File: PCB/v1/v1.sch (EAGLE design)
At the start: 73 parts, among them U2 AT24C512C-SHD-B

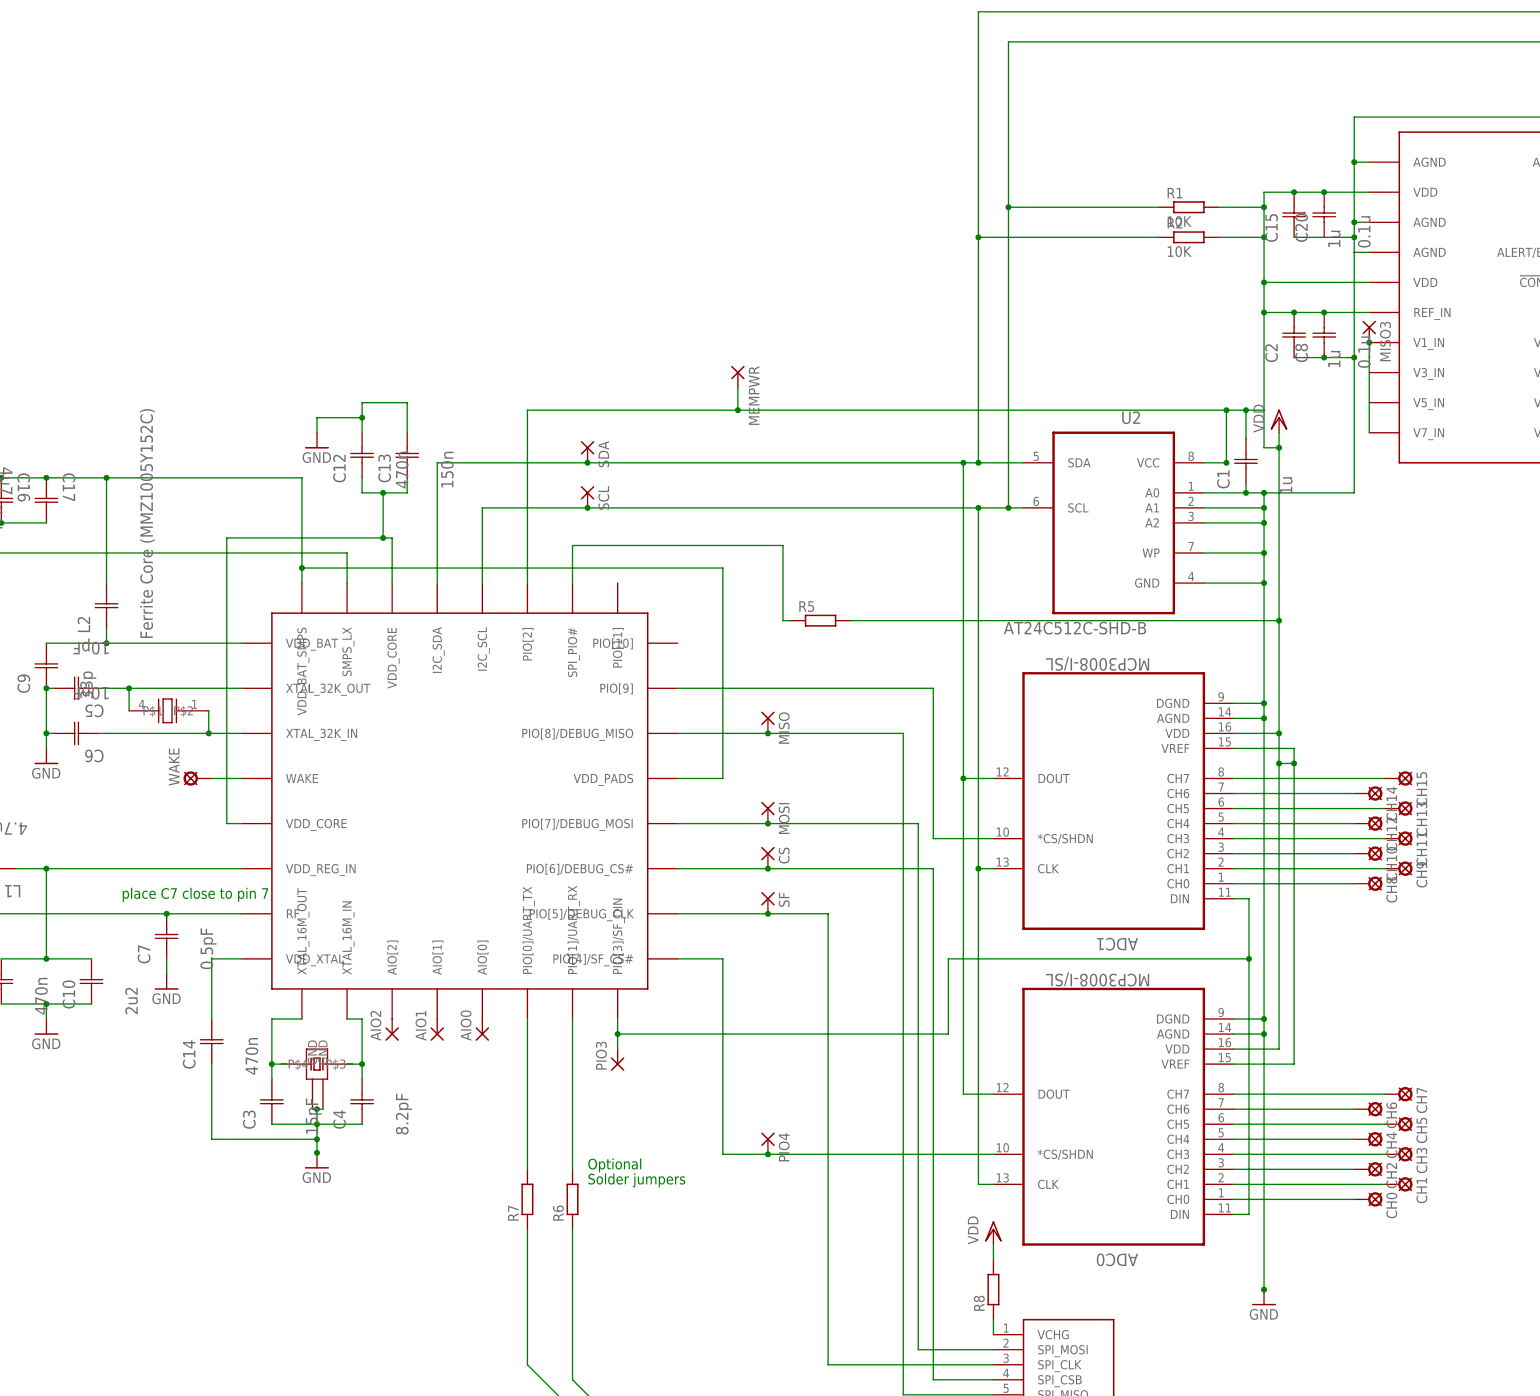
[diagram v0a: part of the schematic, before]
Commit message: ripped up. need to correct ADC package
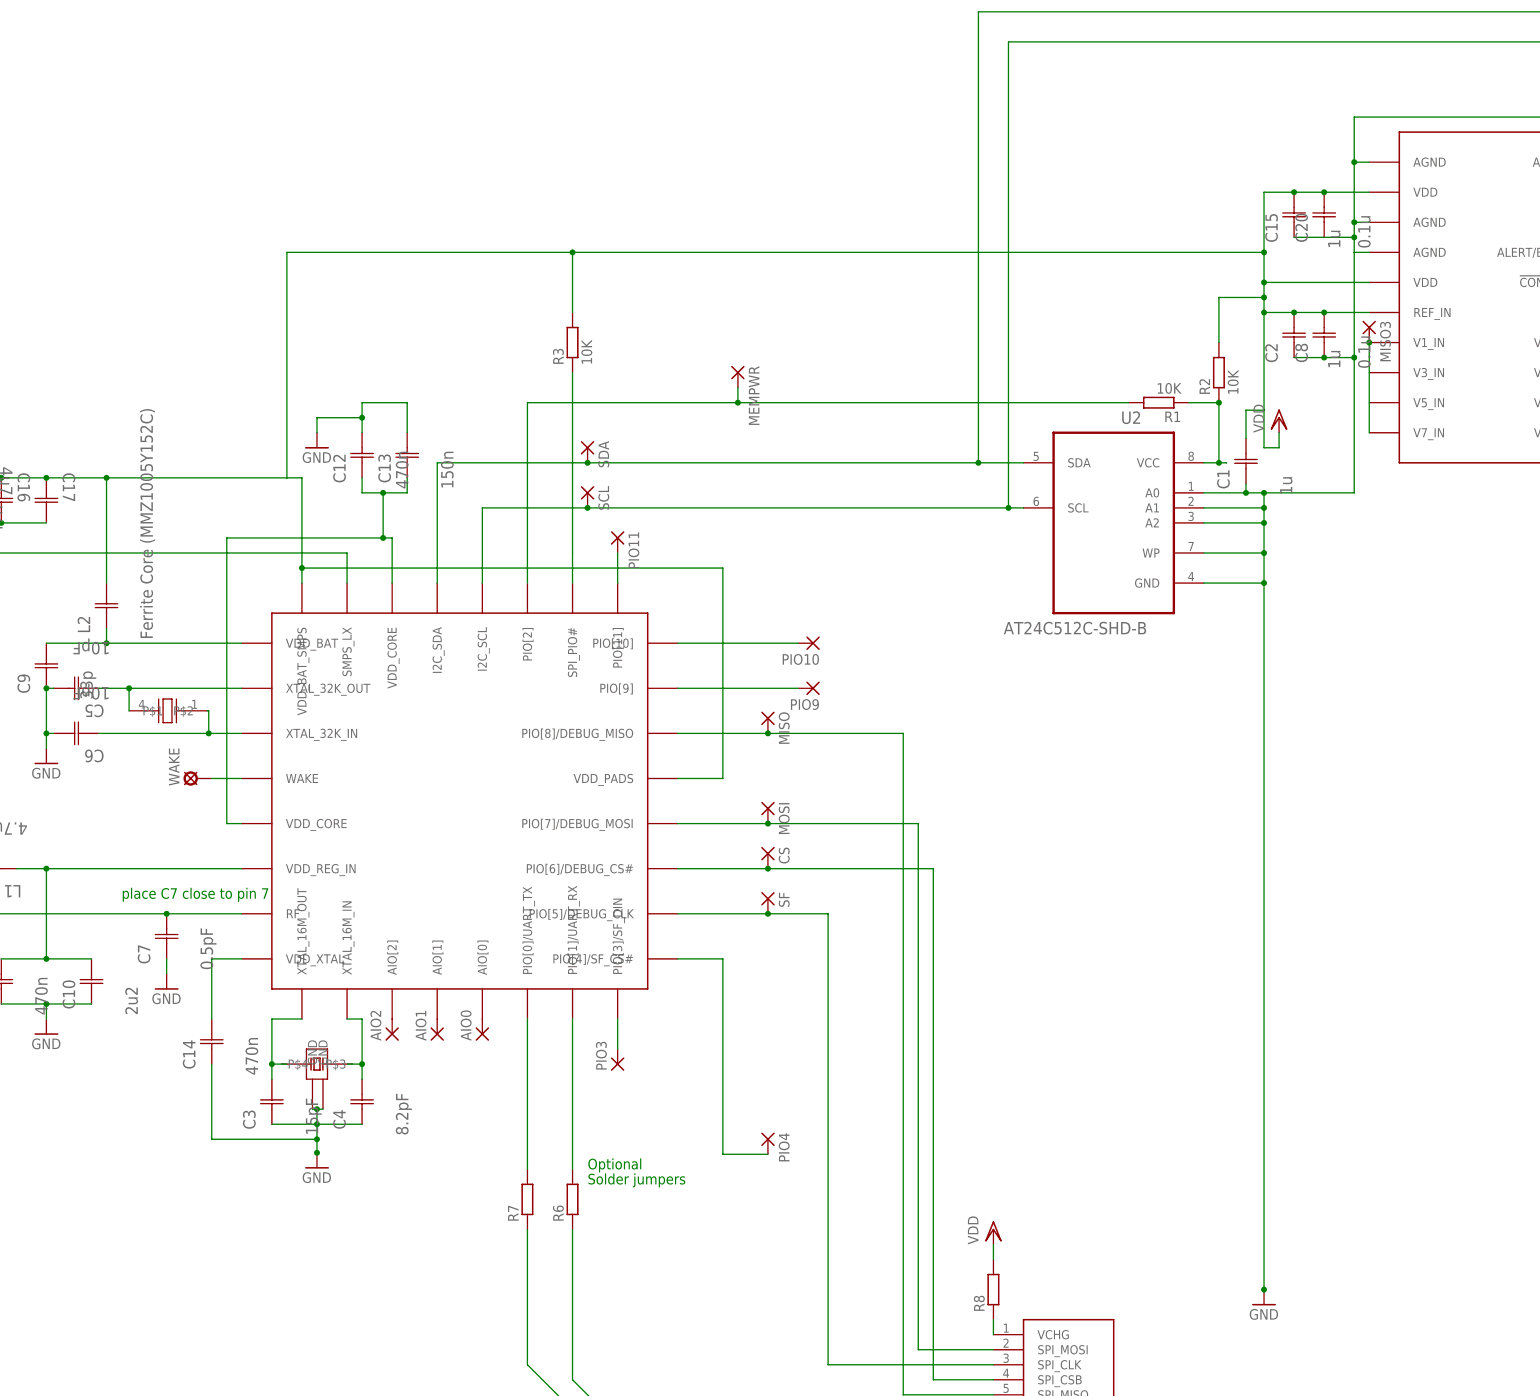
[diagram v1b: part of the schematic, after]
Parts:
- removed ADC0, ADC1: MCP3008-I/SL, Microchip_By_element14_Batch_1:MCP3008-I/SL
- removed CH0, CH1, CH10, CH11, CH12, CH13, CH14, CH15, CH2, CH3, CH4, CH5, CH6, CH7, CH8, CH9: LSP10, solpad:LSP10
- removed R5: (no value), eagle-ltspice:RR1206
- added PIO10, PIO11, PIO9: (no value), wirepad:1,6/0,8
- added R3: 10K, rcl:R-EU_R0402
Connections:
- removed net N$10: ADC1.CH6, CH14.MP
- removed net N$11: ADC1.CH5, CH13.MP
- removed net N$12: ADC1.CH4, CH12.MP
- removed net N$13: ADC1.CH3, CH11.MP
- removed net N$14: ADC1.CH2, CH10.MP
- removed net N$15: ADC1.CH1, CH9.MP
- removed net N$16: ADC1.CH0, CH8.MP
- removed net N$24: ADC1.*CS/SHDN, U$1.PIO[9]
- removed net N$34: C16.C1, C17.C1, C18.C2, C19.C2, L2.C2, U$1.VDD_BAT_SMPS, U$1.VDD_PADS, U$6.POS, VPLUS.MP
- removed net N$6: ADC0.CH2, CH2.MP
- removed net N$7: ADC0.CH1, CH1.MP
- removed net N$8: ADC0.CH0, CH0.MP
- removed net N$9: ADC1.CH7, CH15.MP
- net GND: no longer ADC0.AGND, ADC0.DGND, ADC1.AGND, ADC1.DGND
- net N$1: now also PIO11.P, U$1.PIO[11]; no longer ADC0.CH7, CH7.MP
- net N$2: now also PIO9.P, U$1.PIO[9]; no longer ADC0.CH6, CH6.MP
- net N$23: no longer ADC0.DIN, ADC1.DIN
- net N$25: no longer ADC0.*CS/SHDN
- net N$3: now also MEMPWR.P, R1.2, U$1.PIO[2]; no longer ADC0.CH5, CH5.MP
- net N$4: now also R1.1, R2.1, U2.VCC; no longer ADC0.CH4, CH4.MP
- net N$45: now also R3.1; no longer R5.1
- net N$5: now also PIO10.P, U$1.PIO[10]; no longer ADC0.CH3, CH3.MP
- net SCL: no longer ADC0.CLK, ADC1.CLK, R1.1
- net SDA: no longer ADC0.DOUT, ADC1.DOUT, R2.1
- net VDD: now also C16.C1, C17.C1, C18.C2, C19.C2, L2.C2, R3.2, U$1.VDD_BAT_SMPS, U$1.VDD_PADS, U$6.POS, VPLUS.MP; no longer ADC0.VDD, ADC0.VREF, ADC1.VDD, ADC1.VREF, MEMPWR.P, R1.2, R5.2, U$1.PIO[2], U2.VCC
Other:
- moved on the sheet: R1, R2

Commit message: watanya about to start...
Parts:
- removed U$6: BATTERY_2996, BATTERY_2996:BATTERY_2996
- removed U$7: AD7997, AD7997:AD7997
- U$5: value BATTERY_2996 -> AD7997; device BATTERY_2996:BATTERY_2996 -> AD7997:AD7997
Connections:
- removed net N$48: U$5.POS, U$6.NEG
- net GND: now also U$5.AGND@1, U$5.AGND@2, U$5.AGND@3, U$5.AGND@4, U$5.AS; no longer U$5.NEG, U$7.AGND@1, U$7.AGND@2, U$7.AGND@3, U$7.AGND@4, U$7.AS
- net N$86: now also U$5.V2_IN; no longer U$7.V2_IN
- net N$87: now also U$5.V4_IN; no longer U$7.V4_IN
- net N$88: now also U$5.V1_IN, U$5.V3_IN, U$5.V5_IN, U$5.V7_IN; no longer U$7.V1_IN, U$7.V7_IN
- net N$90: now also U$5.V6_IN, U$5.V8_IN; no longer U$7.V6_IN, U$7.V8_IN
- net SCL: now also U$5.SCL; no longer U$7.SCL
- net SDA: now also U$5.SDA; no longer U$7.SDA
- net VDD: now also U$5.REF_IN, U$5.VDD@1, U$5.VDD@2; no longer U$6.POS, U$7.REF_IN, U$7.VDD@1, U$7.VDD@2
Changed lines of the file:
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@@
 <part name="R8" library="eagle-ltspice" deviceset="R" device="R1206"/>
 <part name="GND" library="ant-planar-1" deviceset="ANTENNA_1" device="LEFT"/>
-<part name="U$5" library="BATTERY_2996" deviceset="BATTERY_2996" device=""/>
-<part name="U$6" library="BATTERY_2996" deviceset="BATTERY_2996" device=""/>
 <part name="U$1" library="CSR1010A05" deviceset="CSR1010A05-IQQM-R" device=""/>
-<part name="U$7" library="AD7997" deviceset="AD7997" device=""/>
 <part name="C2" library="AVX_By_element14_Batch_1" deviceset="UQCL2A100JAT2A/500" device="" value="1u"/>
 <part name="C8" library="AVX_By_element14_Batch_1" deviceset="UQCL2A100JAT2A/500" device="" value="0.1u"/>
@@
 <part name="PIO9" library="wirepad" deviceset="1,6/0,8" device=""/>
 <part name="PIO10" library="wirepad" deviceset="1,6/0,8" device=""/>
+<part name="U$5" library="AD7997" deviceset="AD7997" device=""/>
 </parts>
 <sheets>
@@
 <instance part="R8" gate="G$1" x="30.48" y="-27.94" rot="R90"/>
 <instance part="GND" gate="G$1" x="-157.48" y="45.72"/>
-<instance part="U$5" gate="G$1" x="-172.72" y="78.74"/>
-<instance part="U$6" gate="G$1" x="-172.72" y="101.6"/>
 <instance part="U$1" gate="G$1" x="-58.42" y="55.88"/>
-<instance part="U$7" gate="G$1" x="114.3" y="139.7"/>
 <instance part="C2" gate="A" x="81.28" y="129.54" rot="R90"/>
 <instance part="C8" gate="A" x="86.36" y="129.54" rot="R90"/>
@@
 <instance part="PIO9" gate="P" x="0" y="73.66" rot="R180"/>
 <instance part="PIO10" gate="P" x="0" y="81.28" rot="R180"/>
+<instance part="U$5" gate="G$1" x="114.3" y="139.7"/>
 </instances>
 <busses>
@@
 <junction x="-38.1" y="104.14"/>
 <pinref part="U$1" gate="G$1" pin="I2C_SCL"/>
-<pinref part="U$7" gate="G$1" pin="SCL"/>
 <wire x1="134.62" y1="157.48" x2="139.7" y2="157.48" width="0.1524" layer="91"/>
 <wire x1="139.7" y1="157.48" x2="139.7" y2="182.88" width="0.1524" layer="91"/>
@@
 <junction x="33.02" y="104.14"/>
 <wire x1="33.02" y1="182.88" x2="33.02" y2="104.14" width="0.1524" layer="91"/>
+<pinref part="U$5" gate="G$1" pin="SCL"/>
 </segment>
 </net>
@@
 <wire x1="27.94" y1="187.96" x2="144.78" y2="187.96" width="0.1524" layer="91"/>
 <wire x1="144.78" y1="187.96" x2="144.78" y2="152.4" width="0.1524" layer="91"/>
-<pinref part="U$7" gate="G$1" pin="SDA"/>
 <wire x1="144.78" y1="152.4" x2="134.62" y2="152.4" width="0.1524" layer="91"/>
+<pinref part="U$5" gate="G$1" pin="SDA"/>
 </segment>
 </net>
@@
 <wire x1="91.44" y1="106.68" x2="91.44" y2="129.54" width="0.1524" layer="91"/>
 <junction x="76.2" y="106.68"/>
-<pinref part="U$7" gate="G$1" pin="AGND@3"/>
 <wire x1="91.44" y1="129.54" x2="91.44" y2="147.32" width="0.1524" layer="91"/>
 <wire x1="91.44" y1="147.32" x2="93.98" y2="147.32" width="0.1524" layer="91"/>
@@
 <junction x="86.36" y="129.54"/>
 <junction x="91.44" y="129.54"/>
+<pinref part="U$5" gate="G$1" pin="AGND@3"/>
 </segment>
 <segment>
@@
 <junction x="-154.94" y="101.6"/>
 <junction x="-144.78" y="101.6"/>
-<wire x1="-162.56" y1="71.12" x2="-157.48" y2="71.12" width="0.1524" layer="91"/>
 <wire x1="-157.48" y1="71.12" x2="-157.48" y2="93.98" width="0.1524" layer="91"/>
 <wire x1="-157.48" y1="93.98" x2="-154.94" y2="93.98" width="0.1524" layer="91"/>
 <junction x="-154.94" y="93.98"/>
 <pinref part="VGND" gate="1" pin="MP"/>
-<junction x="-157.48" y="71.12"/>
 <wire x1="-144.78" y1="101.6" x2="-137.16" y2="101.6" width="0.1524" layer="91"/>
-<pinref part="U$5" gate="G$1" pin="NEG"/>
 </segment>
 <segment>
@@
 </segment>
 <segment>
-<pinref part="U$7" gate="G$1" pin="AGND@1"/>
 <wire x1="93.98" y1="162.56" x2="91.44" y2="162.56" width="0.1524" layer="91"/>
 <wire x1="91.44" y1="162.56" x2="91.44" y2="152.4" width="0.1524" layer="91"/>
 <wire x1="91.44" y1="152.4" x2="91.44" y2="149.86" width="0.1524" layer="91"/>
-<pinref part="U$7" gate="G$1" pin="AGND@2"/>
 <wire x1="91.44" y1="149.86" x2="91.44" y2="147.32" width="0.1524" layer="91"/>
 <wire x1="93.98" y1="152.4" x2="91.44" y2="152.4" width="0.1524" layer="91"/>
 <junction x="91.44" y="152.4"/>
-<pinref part="U$7" gate="G$1" pin="AGND@4"/>
 <wire x1="134.62" y1="162.56" x2="134.62" y2="170.18" width="0.1524" layer="91"/>
 <wire x1="134.62" y1="170.18" x2="91.44" y2="170.18" width="0.1524" layer="91"/>
 <wire x1="91.44" y1="170.18" x2="91.44" y2="162.56" width="0.1524" layer="91"/>
 <junction x="91.44" y="162.56"/>
-<pinref part="U$7" gate="G$1" pin="AS"/>
 <wire x1="134.62" y1="137.16" x2="142.24" y2="137.16" width="0.1524" layer="91"/>
 <wire x1="142.24" y1="137.16" x2="142.24" y2="170.18" width="0.1524" layer="91"/>
@@
 <wire x1="81.28" y1="149.86" x2="91.44" y2="149.86" width="0.1524" layer="91"/>
 <junction x="91.44" y="149.86"/>
+<pinref part="U$5" gate="G$1" pin="AGND@1"/>
+<pinref part="U$5" gate="G$1" pin="AGND@2"/>
+<pinref part="U$5" gate="G$1" pin="AS"/>
+<pinref part="U$5" gate="G$1" pin="AGND@4"/>
 </segment>
 </net>
@@
 <pinref part="C1" gate="A" pin="C2"/>
 <wire x1="73.152" y1="120.65" x2="76.2" y2="120.65" width="0.1524" layer="91"/>
-<pinref part="U$7" gate="G$1" pin="VDD@2"/>
 <wire x1="76.2" y1="120.65" x2="76.2" y2="137.16" width="0.1524" layer="91"/>
 <wire x1="76.2" y1="137.16" x2="76.2" y2="139.7" width="0.1524" layer="91"/>
 <wire x1="76.2" y1="139.7" x2="76.2" y2="142.24" width="0.1524" layer="91"/>
 <wire x1="76.2" y1="142.24" x2="93.98" y2="142.24" width="0.1524" layer="91"/>
-<pinref part="U$7" gate="G$1" pin="VDD@1"/>
 <wire x1="93.98" y1="157.48" x2="86.36" y2="157.48" width="0.1524" layer="91"/>
 <wire x1="86.36" y1="157.48" x2="81.28" y2="157.48" width="0.1524" layer="91"/>
@@
 <wire x1="76.2" y1="120.65" x2="76.2" y2="114.3" width="0.1524" layer="91"/>
 <wire x1="76.2" y1="114.3" x2="78.74" y2="114.3" width="0.1524" layer="91"/>
-<pinref part="U$7" gate="G$1" pin="REF_IN"/>
 <wire x1="93.98" y1="137.16" x2="86.36" y2="137.16" width="0.1524" layer="91"/>
 <junction x="76.2" y="137.16"/>
@@
 <junction x="-154.94" y="109.22"/>
 <pinref part="VPLUS" gate="1" pin="MP"/>
-<wire x1="-160.02" y1="109.22" x2="-162.56" y2="109.22" width="0.1524" layer="91"/>
 <wire x1="-160.02" y1="114.3" x2="-160.02" y2="109.22" width="0.1524" layer="91"/>
-<junction x="-160.02" y="109.22"/>
-<pinref part="U$6" gate="G$1" pin="POS"/>
 <pinref part="U$1" gate="G$1" pin="VDD_PADS"/>
 <pinref part="U$1" gate="G$1" pin="VDD_BAT_SMPS"/>
@@
 <wire x1="-40.64" y1="137.16" x2="-40.64" y2="147.32" width="0.1524" layer="91"/>
 <junction x="-40.64" y="147.32"/>
+<pinref part="U$5" gate="G$1" pin="VDD@1"/>
+<pinref part="U$5" gate="G$1" pin="VDD@2"/>
+<pinref part="U$5" gate="G$1" pin="REF_IN"/>
 </segment>
 <segment>
@@
 </segment>
 </net>
-<net name="N$48" class="0">
-<segment>
-<wire x1="-162.56" y1="93.98" x2="-162.56" y2="86.36" width="0.1524" layer="91"/>
-<pinref part="U$5" gate="G$1" pin="POS"/>
-<pinref part="U$6" gate="G$1" pin="NEG"/>
-</segment>
-</net>
 <net name="N$40" class="0">
 <segment>
@@
 <net name="N$86" class="0">
 <segment>
-<pinref part="U$7" gate="G$1" pin="V2_IN"/>
 <pinref part="MISO1" gate="P" pin="P"/>
 <wire x1="134.62" y1="132.08" x2="149.86" y2="132.08" width="0.1524" layer="91"/>
 <wire x1="149.86" y1="132.08" x2="149.86" y2="134.62" width="0.1524" layer="91"/>
+<pinref part="U$5" gate="G$1" pin="V2_IN"/>
 </segment>
 </net>
 <net name="N$87" class="0">
 <segment>
-<pinref part="U$7" gate="G$1" pin="V4_IN"/>
 <pinref part="MISO2" gate="P" pin="P"/>
 <wire x1="134.62" y1="127" x2="149.86" y2="127" width="0.1524" layer="91"/>
+<pinref part="U$5" gate="G$1" pin="V4_IN"/>
 </segment>
 </net>
 <net name="N$88" class="0">
 <segment>
-<pinref part="U$7" gate="G$1" pin="V1_IN"/>
 <pinref part="MISO3" gate="P" pin="P"/>
-<pinref part="U$7" gate="G$1" pin="V7_IN"/>
-<wire x1="93.98" y1="116.84" x2="93.98" y2="132.08" width="0.1524" layer="91"/>
+<wire x1="93.98" y1="116.84" x2="93.98" y2="121.92" width="0.1524" layer="91"/>
+<pinref part="U$5" gate="G$1" pin="V1_IN"/>
 <junction x="93.98" y="132.08"/>
+<pinref part="U$5" gate="G$1" pin="V3_IN"/>
+<wire x1="93.98" y1="121.92" x2="93.98" y2="127" width="0.1524" layer="91"/>
+<wire x1="93.98" y1="127" x2="93.98" y2="132.08" width="0.1524" layer="91"/>
+<junction x="93.98" y="127"/>
+<pinref part="U$5" gate="G$1" pin="V5_IN"/>
+<junction x="93.98" y="121.92"/>
+<pinref part="U$5" gate="G$1" pin="V7_IN"/>
 </segment>
 </net>
 <net name="N$90" class="0">
 <segment>
-<pinref part="U$7" gate="G$1" pin="V8_IN"/>
-<pinref part="U$7" gate="G$1" pin="V6_IN"/>
 <wire x1="134.62" y1="116.84" x2="134.62" y2="119.38" width="0.1524" layer="91"/>
 <wire x1="134.62" y1="119.38" x2="134.62" y2="121.92" width="0.1524" layer="91"/>
 <wire x1="134.62" y1="119.38" x2="142.24" y2="119.38" width="0.1524" layer="91"/>
 <junction x="134.62" y="119.38"/>
-</segment>
-</net>
+<pinref part="U$5" gate="G$1" pin="V8_IN"/>
+<pinref part="U$5" gate="G$1" pin="V6_IN"/>
+</segment>
+</net>
